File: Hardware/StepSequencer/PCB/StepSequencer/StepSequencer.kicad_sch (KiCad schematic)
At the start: 54 parts, among them J1 Conn_01x04_Male, SW1 SW_DIP_x01, SW10 SW_DIP_x01, SW11 SW_DIP_x01, SW12 SW_DIP_x01, SW13 SW_DIP_x01, SW14 SW_DIP_x01, SW15 SW_DIP_x01, SW16 SW_DIP_x01, SW17 SW_DIP_x01, SW18 SW_DIP_x01, SW19 SW_DIP_x01, SW2 SW_DIP_x01, SW20 SW_DIP_x01, SW21 SW_DIP_x01, SW22 SW_DIP_x01, SW23 SW_DIP_x01, SW3 SW_DIP_x01, SW4 SW_DIP_x01, SW5 SW_DIP_x01, SW6 SW_DIP_x01, SW7 SW_DIP_x01, SW8 SW_DIP_x01, SW9 SW_DIP_x01, U1 MCP23017_SP

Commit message: Initial test for StepSequencer
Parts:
- renumbered RR3 to R3
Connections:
- net GPA0: now also SW10.1, SW11.1, SW6.1, SW7.1, SW8.1, SW9.1; no longer SW18.1, SW19.1, SW20.1, SW21.1, SW22.1, SW23.1
- net GPA2: now also SW12.1, SW13.1, SW14.1, SW15.1, SW16.1, SW17.1; no longer SW10.1, SW11.1, SW6.1, SW7.1, SW8.1, SW9.1
- net GPA3: now also SW18.1, SW19.1, SW20.1, SW21.1, SW22.1, SW23.1; no longer R6.1
- net GPA4: now also R6.1; no longer SW12.1, SW13.1, SW14.1, SW15.1, SW16.1, SW17.1
- net GPA6: now also R5.1; no longer SW1.1, SW2.1, SW3.1, SW4.1, SW5.1
- net GPA7: now also SW1.1, SW2.1, SW3.1, SW4.1, SW5.1; no longer R5.1
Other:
- title: (none) -> Daisy Seed Development Kit Step Sequencer

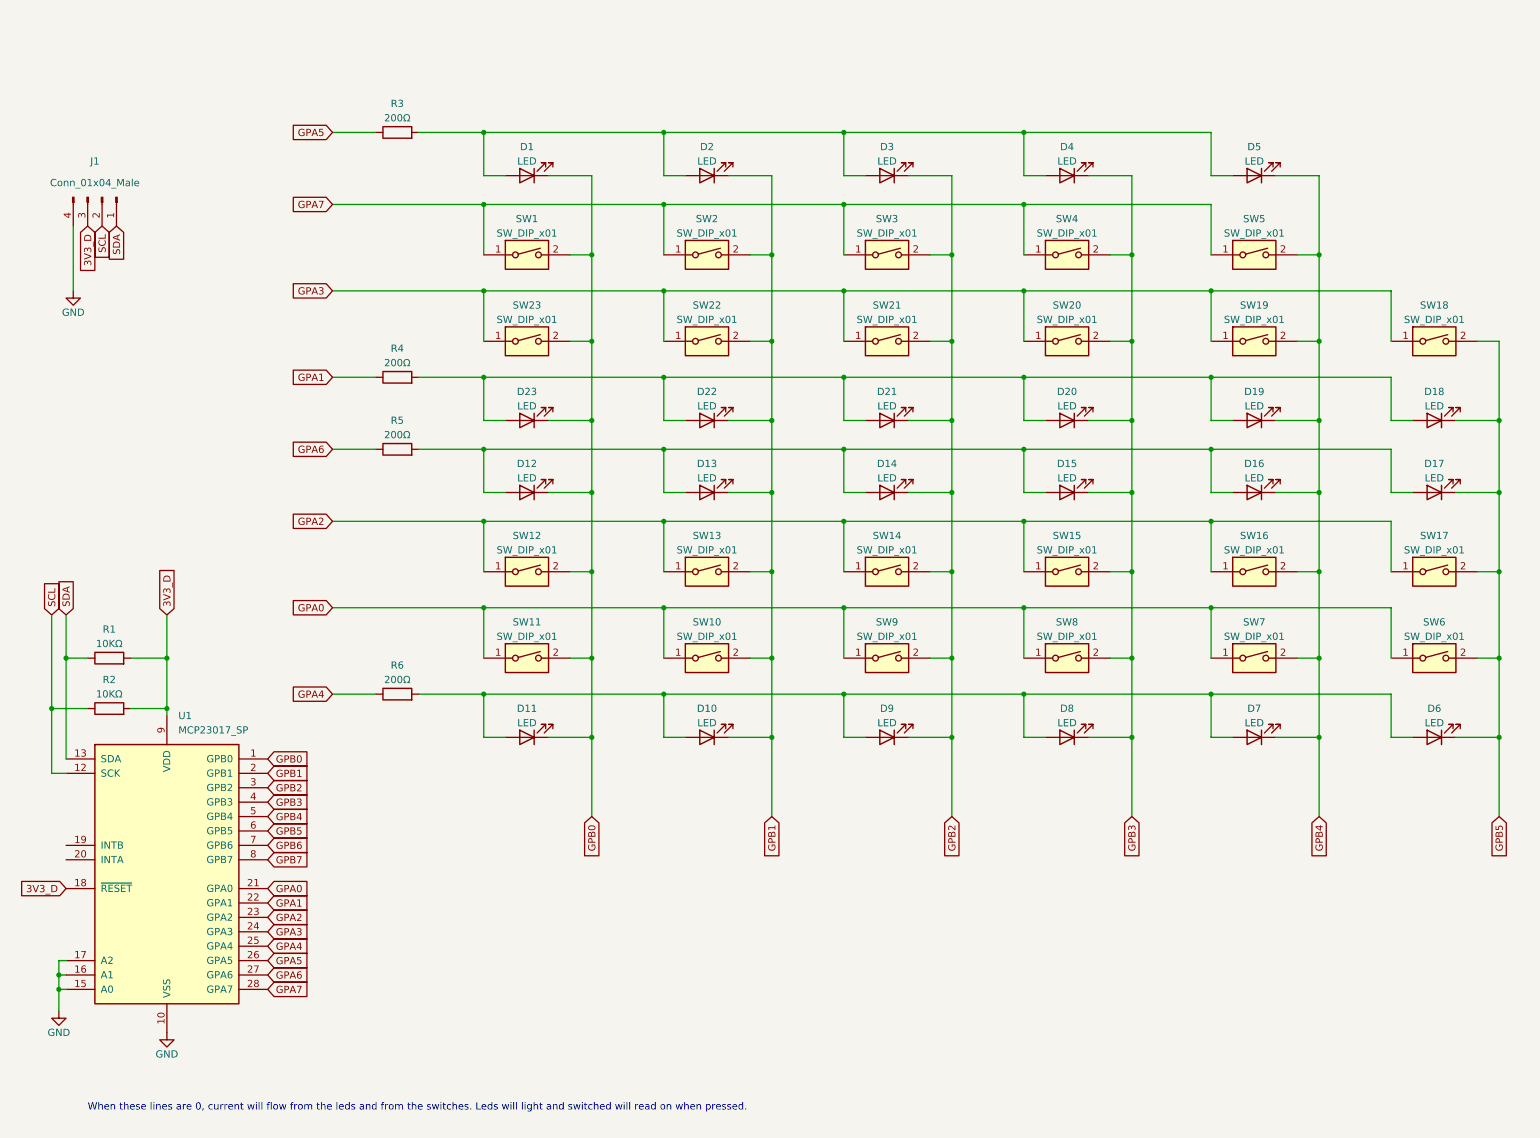
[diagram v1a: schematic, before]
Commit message: Recording multiple key press and tart of new hardware
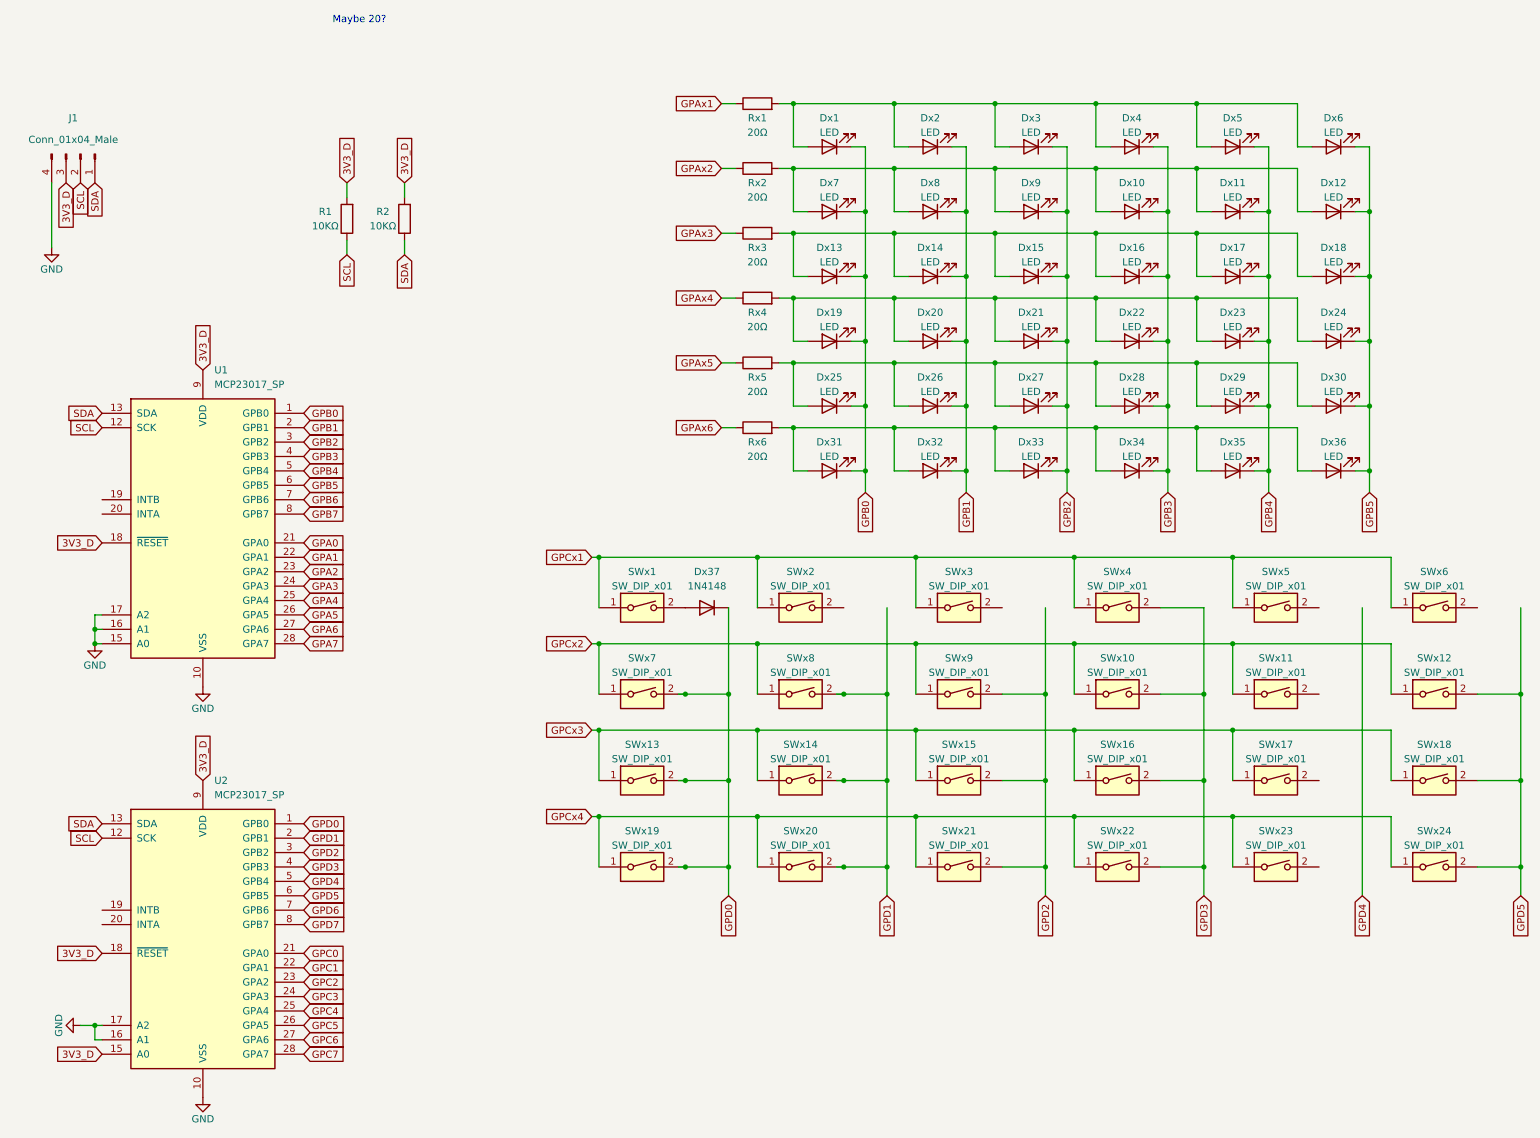
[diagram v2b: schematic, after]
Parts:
- removed D1, D10, D11, D12, D13, D14, D15, D16, D17, D18, D19, D2, D20, D21, D22, D23, D3, D4, D5, D6, D7, D8, D9: LED, LED_THT:LED_D3.0mm, symbol Device:LED
- removed R3, R4, R5, R6: 200Ω, Resistor_THT:R_Axial_DIN0207_L6.3mm_D2.5mm_P10.16mm_Horizontal, symbol Device:R
- removed SW1, SW10, SW11, SW12, SW13, SW14, SW15, SW16, SW17, SW18, SW19, SW2, SW20, SW21, SW22, SW23, SW3, SW4, SW5, SW6, SW7, SW8, SW9: SW_DIP_x01, Button_Switch_THT:SW_PUSH_6mm, symbol Switch:SW_DIP_x01
- added Dx1, Dx10, Dx11, Dx12, Dx13, Dx14, Dx15, Dx16, Dx17, Dx18, Dx19, Dx2, Dx20, Dx21, Dx22, Dx23, Dx24, Dx25, Dx26, Dx27, Dx28, Dx29, Dx3, Dx30, Dx31, Dx32, Dx33, Dx34, Dx35, Dx36, Dx4, Dx5, Dx6, Dx7, Dx8, Dx9: LED, LED_THT:LED_D3.0mm, symbol Device:LED
- added Dx37: 1N4148, Diode_THT:D_DO-35_SOD27_P7.62mm_Horizontal, symbol Diode:1N4148
- added Rx1, Rx2, Rx3, Rx4, Rx5, Rx6: 20Ω, Resistor_THT:R_Axial_DIN0207_L6.3mm_D2.5mm_P10.16mm_Horizontal, symbol Device:R
- added SWx1, SWx10, SWx11, SWx12, SWx13, SWx14, SWx15, SWx16, SWx17, SWx18, SWx19, SWx2, SWx20, SWx21, SWx22, SWx23, SWx24, SWx3, SWx4, SWx5, SWx6, SWx7, SWx8, SWx9: SW_DIP_x01, Button_Switch_THT:SW_PUSH_6mm, symbol Switch:SW_DIP_x01
- added U2: MCP23017_SP, Package_DIP:DIP-28_W7.62mm, symbol Interface_Expansion:MCP23017_SP
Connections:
- net 3V3_D: now also U2.15 (A0), U2.18 (~{RESET}), U2.9 (VDD)
- net GND: now also U2.10 (VSS), U2.16 (A1), U2.17 (A2)
- net GPB0: now also Dx1.1 (K), Dx13.1 (K), Dx19.1 (K), Dx25.1 (K), Dx31.1 (K), Dx7.1 (K)
- net GPB1: now also Dx14.1 (K), Dx2.1 (K), Dx20.1 (K), Dx26.1 (K), Dx32.1 (K), Dx8.1 (K)
- net GPB2: now also Dx15.1 (K), Dx21.1 (K), Dx27.1 (K), Dx3.1 (K), Dx33.1 (K), Dx9.1 (K)
- net GPB3: now also Dx10.1 (K), Dx16.1 (K), Dx22.1 (K), Dx28.1 (K), Dx34.1 (K), Dx4.1 (K)
- net GPB4: now also Dx11.1 (K), Dx17.1 (K), Dx23.1 (K), Dx29.1 (K), Dx35.1 (K), Dx5.1 (K)
- net GPB5: now also Dx12.1 (K), Dx18.1 (K), Dx24.1 (K), Dx30.1 (K), Dx36.1 (K), Dx6.1 (K)
- net SCL: now also R1.1, U2.12 (SCK); no longer R2.1
- net SDA: now also R2.1, U2.13 (SDA); no longer R1.1
- new net: Dx1.2 (A), Dx2.2 (A), Dx3.2 (A), Dx4.2 (A), Dx5.2 (A), Dx6.2 (A), Rx1.2
- new net: Dx13.2 (A), Dx14.2 (A), Dx15.2 (A), Dx16.2 (A), Dx17.2 (A), Dx18.2 (A), Rx3.2
- new net: Dx31.2 (A), Dx32.2 (A), Dx33.2 (A), Dx34.2 (A), Dx35.2 (A), Dx36.2 (A), Rx6.2
- new net: Dx10.2 (A), Dx11.2 (A), Dx12.2 (A), Dx7.2 (A), Dx8.2 (A), Dx9.2 (A), Rx2.2
- new net: Dx19.2 (A), Dx20.2 (A), Dx21.2 (A), Dx22.2 (A), Dx23.2 (A), Dx24.2 (A), Rx4.2
- new net: Dx25.2 (A), Dx26.2 (A), Dx27.2 (A), Dx28.2 (A), Dx29.2 (A), Dx30.2 (A), Rx5.2
- new net: Dx37.2 (A), SWx1.2
- new net GPAx1: Rx1.1
- new net GPAx2: Rx2.1
- new net GPAx3: Rx3.1
- new net GPAx4: Rx4.1
- new net GPAx5: Rx5.1
- new net GPAx6: Rx6.1
- new net GPC0: U2.21 (GPA0)
- new net GPC1: U2.22 (GPA1)
- new net GPC2: U2.23 (GPA2)
- new net GPC3: U2.24 (GPA3)
- new net GPC4: U2.25 (GPA4)
- new net GPC5: U2.26 (GPA5)
- new net GPC6: U2.27 (GPA6)
- new net GPC7: U2.28 (GPA7)
- new net GPCx1: SWx1.1, SWx2.1, SWx3.1, SWx4.1, SWx5.1, SWx6.1
- new net GPCx2: SWx10.1, SWx11.1, SWx12.1, SWx7.1, SWx8.1, SWx9.1
- new net GPCx3: SWx13.1, SWx14.1, SWx15.1, SWx16.1, SWx17.1, SWx18.1
- new net GPCx4: SWx19.1, SWx20.1, SWx21.1, SWx22.1, SWx23.1, SWx24.1
- new net GPD0: Dx37.1 (K), SWx13.2, SWx19.2, SWx7.2, U2.1 (GPB0)
- new net GPD1: SWx14.2, SWx20.2, SWx8.2, U2.2 (GPB1)
- new net GPD2: SWx15.2, SWx21.2, SWx9.2, U2.3 (GPB2)
- new net GPD3: SWx10.2, SWx16.2, SWx22.2, SWx4.2, U2.4 (GPB3)
- new net GPD4: U2.5 (GPB4)
- new net GPD5: SWx12.2, SWx18.2, SWx24.2, U2.6 (GPB5)
- new net GPD6: U2.7 (GPB6)
- new net GPD7: U2.8 (GPB7)
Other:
- note added: "Maybe 20?"
- note removed: "When these lines are 0, current will flow from the leds and from the switches. Leds will light and switched will read on when pressed."
- moved on the sheet: J1, U1

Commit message: Hardware update
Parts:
- removed Dx31: LED, LED_THT:LED_D3.0mm, symbol Device:LED
- removed Dx37: 1N4148, Diode_THT:D_DO-35_SOD27_P7.62mm_Horizontal, symbol Diode:1N4148
- removed SWx19: SW_DIP_x01, Button_Switch_THT:SW_PUSH_6mm, symbol Switch:SW_DIP_x01
- renumbered Dx26 to D1, Dx36 to D10, Dx22 to D11, Dx35 to D12, Dx34 to D13, Dx23 to D14, Dx33 to D15, Dx24 to D16, Dx32 to D17, Dx1 to D18, Dx2 to D19, Dx25 to D2, Dx3 to D20, Dx4 to D21, Dx5 to D22, Dx6 to D23, Dx12 to D24, Dx11 to D25, Dx10 to D26, Dx9 to D27, Dx8 to D28, Dx7 to D29, Dx27 to D3, Dx13 to D30, Dx14 to D31, Dx15 to D32, Dx16 to D33, Dx17 to D34, Dx18 to D35, Dx19 to D4, Dx28 to D5, Dx29 to D6, Dx20 to D7, Dx30 to D8, Dx21 to D9, Rx6 to R3, Rx5 to R4, Rx4 to R5, Rx1 to R6, Rx2 to R7, Rx3 to R8, SWx9 to SW1, SWx15 to SW10, SWx5 to SW11, SWx16 to SW12, SWx17 to SW13, SWx4 to SW14, SWx18 to SW15, SWx3 to SW16, SWx24 to SW17, SWx2 to SW18, SWx1 to SW19, SWx10 to SW2, SWx20 to SW20, SWx21 to SW21, SWx23 to SW22, SWx22 to SW23, SWx8 to SW3, SWx11 to SW4, SWx7 to SW5, SWx13 to SW6, SWx12 to SW7, SWx14 to SW8, SWx6 to SW9
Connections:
- net GPAx1 is gone; now on net GPA5: R6.1
- net GPAx2 is gone; now on net GPA6: R7.1
- net GPAx3 is gone; now on net GPA7: R8.1
- net GPAx4 is gone; now on net GPA4: R5.1
- net GPAx5 is gone; now on net GPA3: R4.1
- net GPAx6 is gone; now on net GPA2: R3.1
- net GPCx1 is gone; now on net GPC4: SW11.1, SW14.1, SW16.1, SW18.1, SW19.1, SW9.1
- net GPCx2 is gone; now on net GPC5: SW1.1, SW2.1, SW3.1, SW4.1, SW5.1, SW7.1
- net GPCx3 is gone; now on net GPC6: SW10.1, SW12.1, SW13.1, SW15.1, SW6.1, SW8.1
- net GPCx4 is gone; now on net GPC7: SW17.1, SW20.1, SW21.1, SW22.1, SW23.1
- net GPD0: now also SW15.2, SW17.2, SW7.2, SW9.2; no longer SW5.2, SW6.2
- net GPD1: now also SW11.2, SW13.2, SW22.2, SW4.2; no longer SW20.2, SW3.2, SW8.2
- net GPD2: now also SW12.2, SW14.2, SW2.2, SW23.2; no longer SW1.2, SW10.2, SW21.2
- net GPD3: now also SW1.2, SW10.2, SW16.2, SW21.2; no longer SW12.2, SW14.2, SW2.2, SW23.2
- net GPD4: now also SW18.2, SW20.2, SW3.2, SW8.2
- net GPD5: now also SW19.2, SW5.2, SW6.2; no longer SW15.2, SW17.2, SW7.2
